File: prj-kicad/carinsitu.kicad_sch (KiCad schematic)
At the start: 65 parts, among them P1 BAT, P2 MOT, P3 CONN_3, P4 CONN_4, SW1 SWITCH_SLIDE, SW2 SW_Push, U1 LoLin_D1_mini_pro, U2 MIC2860, U3 MAX17205, U4 SN74LVC1T45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

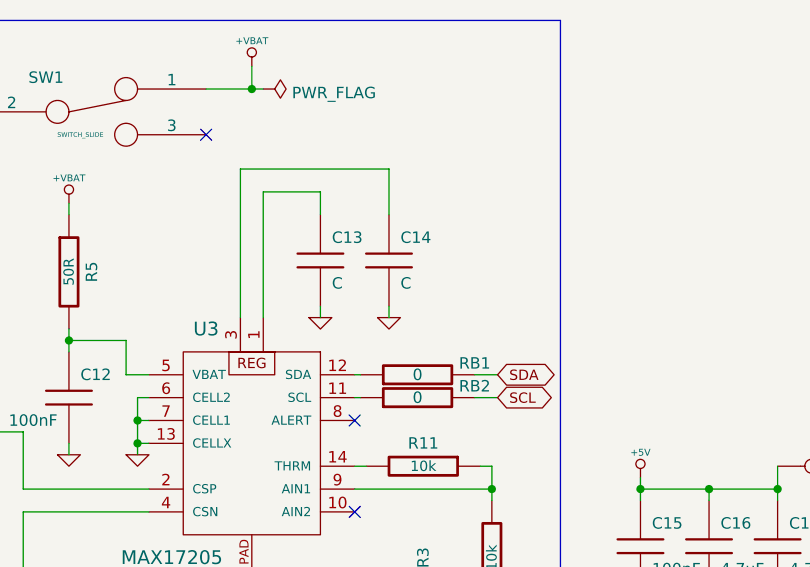
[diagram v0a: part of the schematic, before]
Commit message: review MAX17205 Fuel Gauge Add missing cap values
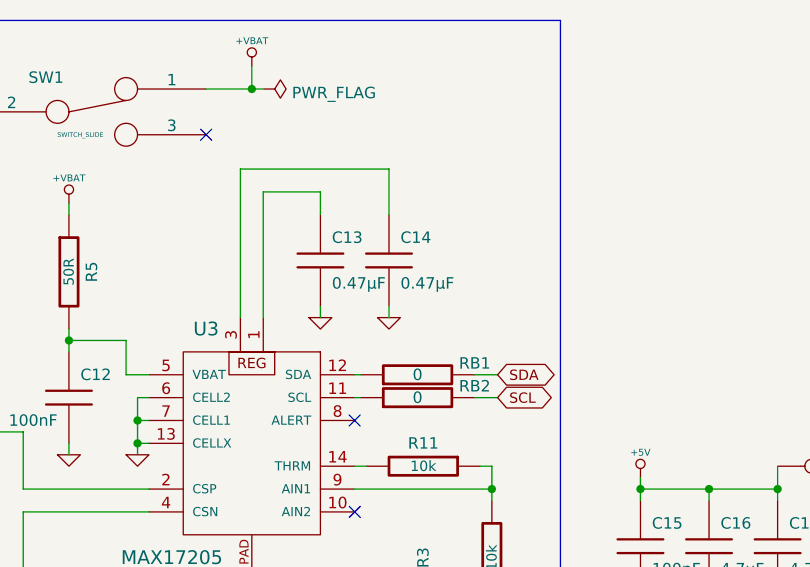
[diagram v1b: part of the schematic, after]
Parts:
- C13, C14: value C -> 0.47µF
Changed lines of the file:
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@@
       (effects (font (size 1.27 1.27)) (justify left))
     )
-    (property "Value" "C" (id 1) (at 74.93 149.86 0)
+    (property "Value" "0.47µF" (id 1) (at 74.93 149.86 0)
       (effects (font (size 1.27 1.27)) (justify left))
     )
@@
       (effects (font (size 1.27 1.27)) (justify left))
     )
-    (property "Value" "C" (id 1) (at 82.55 149.86 0)
+    (property "Value" "0.47µF" (id 1) (at 82.55 149.86 0)
       (effects (font (size 1.27 1.27)) (justify left))
     )
@@
     )
     (path "/00000000-0000-0000-0000-00005d26d447"
-      (reference "C13") (unit 1) (value "C") (footprint "carinsitu:SMD0603")
+      (reference "C13") (unit 1) (value "0.47µF") (footprint "carinsitu:SMD0603")
     )
     (path "/00000000-0000-0000-0000-00005d26d4c0"
-      (reference "C14") (unit 1) (value "C") (footprint "carinsitu:SMD0603")
+      (reference "C14") (unit 1) (value "0.47µF") (footprint "carinsitu:SMD0603")
     )
     (path "/00000000-0000-0000-0000-00005d2c6e10"

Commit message: Update PCB + schematic adjustments
Notable schematic changes:
- change level shifters for SN74LV1T34DBV (simplify routing)
- add fuse inversion protection
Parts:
- removed U4, U8: SN74LVC1T45, carinsitu:SOT23-6, symbol carinsitu:SN74LVC1T45
- added D3: D, Diode_THT:D_A-405_P2.54mm_Vertical_KathodeUp, symbol Device:D
- added F1: Polyfuse, Fuse:Fuse_Bourns_MF-RG500, symbol Device:Polyfuse
- added R14: 10k, carinsitu:SMD0805, symbol carinsitu:R
- added U4, U5: SN74LV1T34DBV, Package_TO_SOT_SMD:SOT-23-5, symbol Logic_LevelTranslator:SN74LV1T34DBV
- C4: value 100nF -> 4.7uF
- R11: footprint carinsitu:SMD0603 -> carinsitu:SMD0805
- RB1, RB2, RB3, RB4, RB5, RB6, RB7, RB8, RB9: footprint (none) -> carinsitu:SMD0603
- SW2: value SW_Push -> Reset
- TP12: value CONN_1 -> INT2
- TP13: value CONN_1 -> INT1
- TP7: value CONN_1 -> PPM_ESC
- TP8: value CONN_1 -> HL_PWM
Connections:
- net +5V: now also U4.5 (VCC), U5.5 (VCC)
- net +VBAT: now also SW1.3; no longer SW1.1
- net GND: now also R14.1, U4.3 (GND), U5.3 (GND)
- net PPM_SERVO: now also U4.2 (A); no longer TP6.1
- net RL_DAT: now also R14.2, U5.2 (A); no longer TP9.1
- net at P1.1 (P1): now also R4.1, U3.2 (CSP), D3.2 (A); no longer SW1.2
- net at P3.1 (P1): now also TP6.1, U4.4 (Y)
- net at D4.4 (DIN): now also TP9.1, U5.4 (Y)
- new net: F1.2, P1.2 (PM)
- new net: D3.1 (K), F1.1, SW1.2
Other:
- note added: "Note: MCU has pullup"
- moved on the sheet: C3, C4, D4, D5, P1, P3, RB8, RB9, SW1, TP12, TP13, TP6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

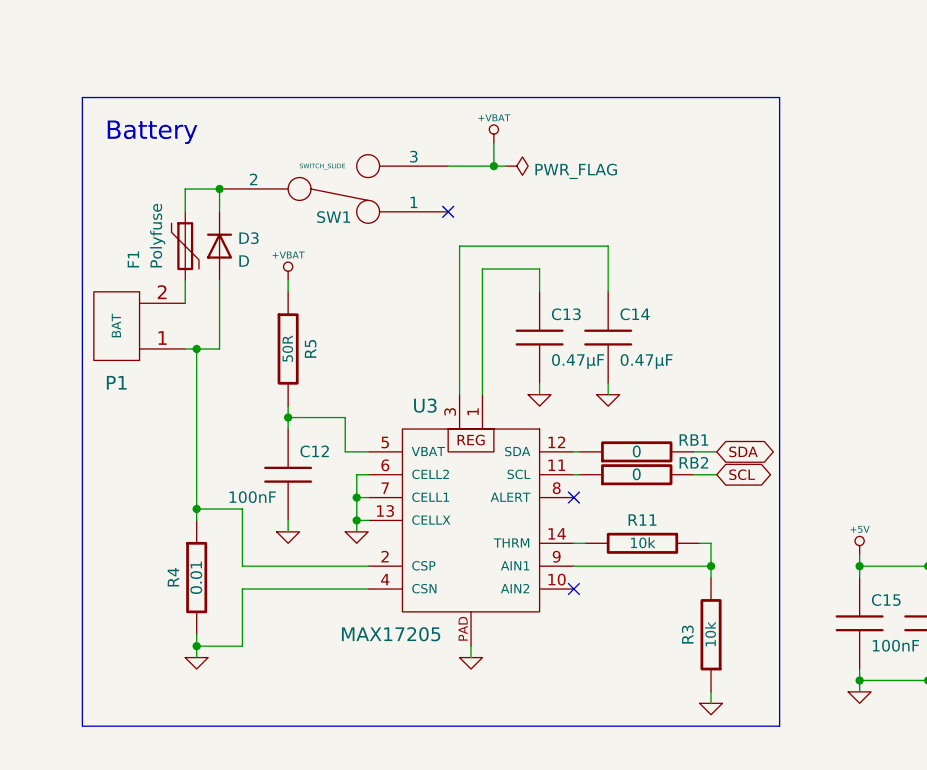
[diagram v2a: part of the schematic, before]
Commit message: Change battery monitor MAX17044G in schematic
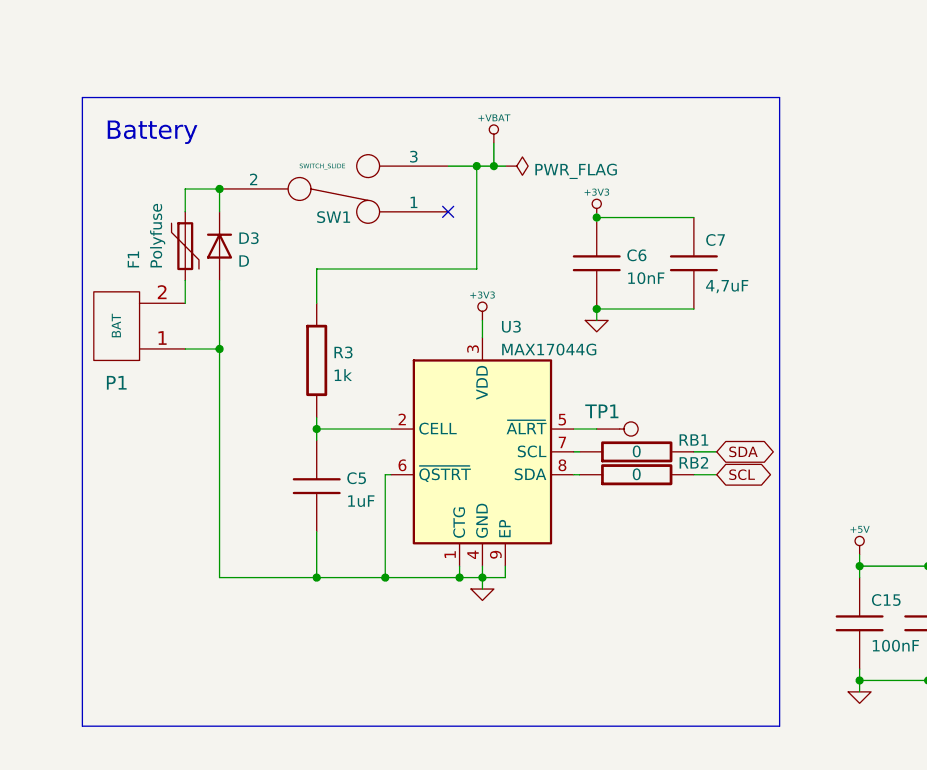
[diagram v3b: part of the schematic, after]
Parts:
- removed C12: 100nF, carinsitu:SMD0603, symbol carinsitu:C
- removed C13, C14: 0.47µF, carinsitu:SMD0603, symbol carinsitu:C
- removed R11: 10k, carinsitu:SMD0805, symbol carinsitu:R
- removed R4: 0.01, carinsitu:SMD0805, symbol carinsitu:R
- removed R5: 50R, carinsitu:SMD0603, symbol carinsitu:R
- removed U3: MAX17205, carinsitu:TDFN14, symbol carinsitu:MAX17205
- added C5: 1uF, carinsitu:SMD0805, symbol carinsitu:C
- added C6: 10nF, carinsitu:SMD0603, symbol carinsitu:C
- added C7: 4,7uF, carinsitu:SMD0805, symbol carinsitu:C
- added TP1: CONN_1, carinsitu:TP, symbol carinsitu:CONN_1
- added U3: MAX17044G, Package_DFN_QFN:TDFN-8-1EP_3x2mm_P0.5mm_EP1.80x1.65mm, symbol carinsitu:MAX17044G
- R3: value 10k -> 1k
- TP12: value INT2 -> CONN_1; RefBis (none) -> INT2
- TP13: value INT1 -> CONN_1; RefBis (none) -> INT1
- TP7: value PPM_ESC -> CONN_1; RefBis (none) -> PPM_ESC
- TP8: value HL_PWM -> CONN_1; RefBis (none) -> HL_PWM
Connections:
- net +3V3: now also C6.1, C7.1, U3.3 (VDD)
- net +VBAT: now also R3.1
- net GND: now also D3.2 (A), P1.1 (P1), C5.2, C6.2, C7.2, U3.1 (CTG), U3.4 (GND), U3.6 (~{QSTRT}), U3.9 (EP); no longer R3.1
- net at R3.2: now also C5.1, U3.2 (CELL)
- net at RB2.1: now also U3.8 (SDA)
- net at RB1.1: now also U3.7 (SCL)
- new net: TP1.1, U3.5 (~{ALRT})
- no-connect marks 6 -> 4

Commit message: Change some footprints for kicad lib ones + silkscreen + route adjustments
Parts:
- C1, C16, C17, C5, C7: footprint carinsitu:SMD0805 -> Capacitor_SMD:C_0805_2012Metric
- C15, C2, C3, C6: footprint carinsitu:SMD0603 -> Capacitor_SMD:C_0603_1608Metric
- C4: footprint carinsitu:SMD0603 -> Capacitor_SMD:C_0805_2012Metric
- D1, D2: footprint carinsitu:LED -> LED_THT:LED_D5.0mm_Horizontal_O3.81mm_Z3.0mm
- R1, R10, R12, R14, R2, R3, R6, R7, R8, R9: footprint carinsitu:SMD0805 -> Resistor_SMD:R_0805_2012Metric
- RB1, RB2, RB3, RB4, RB5, RB6, RB7, RB8, RB9: footprint carinsitu:SMD0603 -> Resistor_SMD:R_0603_1608Metric
- U2: footprint carinsitu:SOT23-6 -> Package_TO_SOT_SMD:SOT-23-6

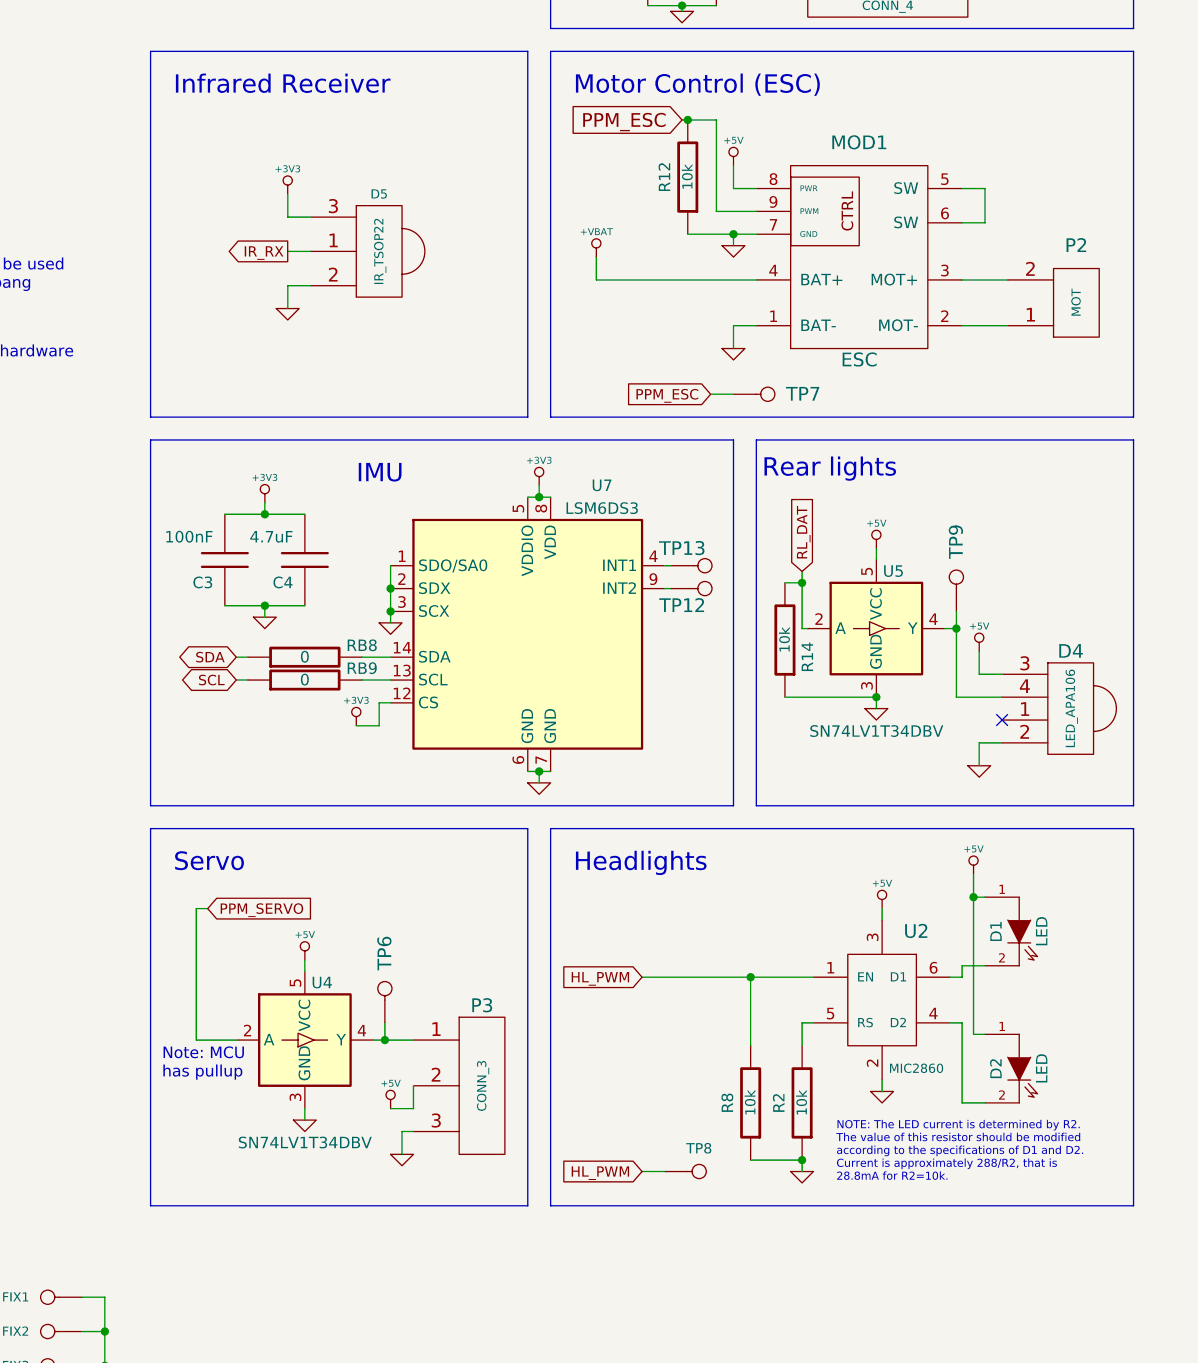
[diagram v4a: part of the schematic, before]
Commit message: Add decoupling capacitors + RB10
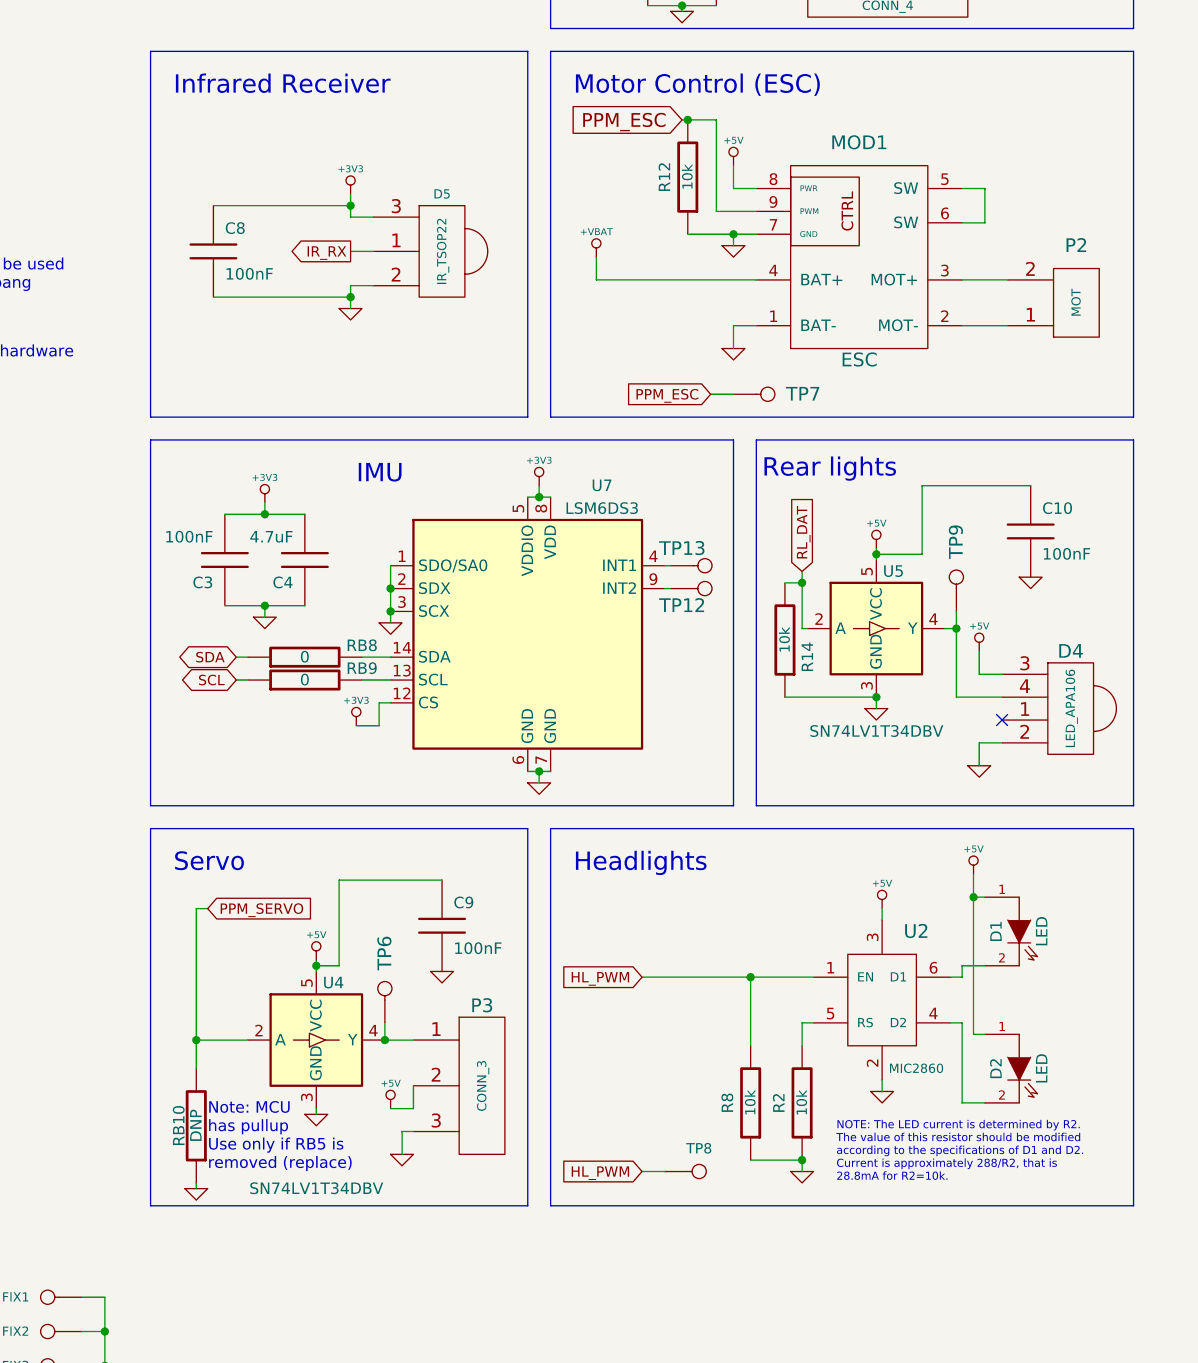
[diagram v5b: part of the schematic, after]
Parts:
- added C10, C8, C9: 100nF, Capacitor_SMD:C_0603_1608Metric, symbol carinsitu:C
- added RB10: DNP, Resistor_SMD:R_0603_1608Metric, symbol carinsitu:R
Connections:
- net +3V3: now also C8.1
- net +5V: now also C10.1, C9.1
- net GND: now also C10.2, C8.2, C9.2, RB10.1
- net PPM_SERVO: now also RB10.2
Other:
- note added: "Note: MCU has pullup Use only if RB5 is removed (replace)"
- note removed: "Note: MCU has pullup"
- moved on the sheet: D5, U4

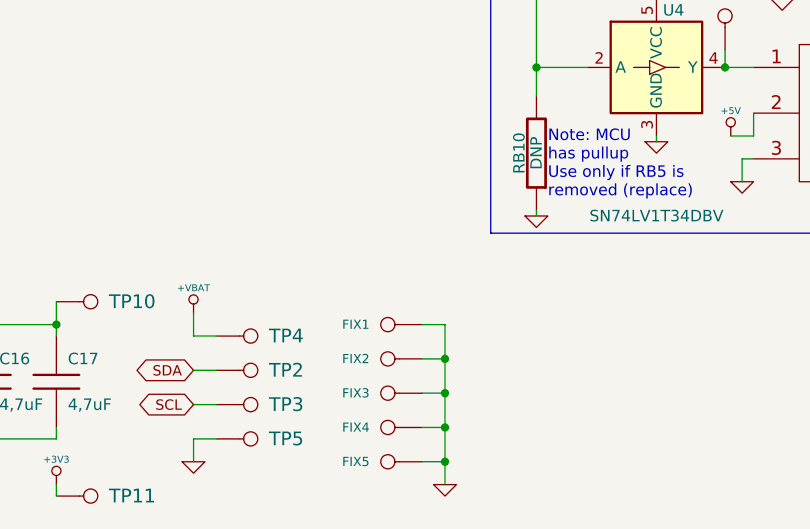
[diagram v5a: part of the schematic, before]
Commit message: Add VTX holes (WIP, bottom right needs rerouting)
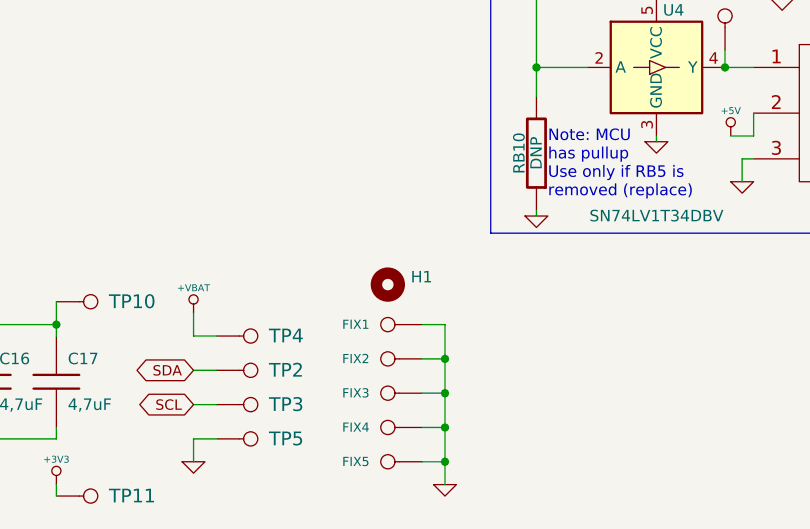
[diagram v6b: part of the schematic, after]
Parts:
- added H1: MountingHole, symbol Mechanical:MountingHole
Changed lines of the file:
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@@
     (pin "1")
+  )
+  (symbol (lib_id "Mechanical:MountingHole") (at 161.29 168.275 0) (unit 1)
+    (in_bom yes) (on_board yes) (fields_autoplaced)
+    (property "Reference" "H1" (id 0) (at 163.83 167.4403 0)
+      (effects (font (size 1.27 1.27)) (justify left))
+    )
+    (property "Value" "MountingHole" (id 1) (at 163.83 169.9772 0)
+      (effects (font (size 1.27 1.27)) (justify left) hide)
+    )
+    (property "Footprint" "" (id 2) (at 161.29 168.275 0)
+      (effects (font (size 1.27 1.27)) hide)
+    )
+    (property "Datasheet" "~" (id 3) (at 161.29 168.275 0)
+      (effects (font (size 1.27 1.27)) hide)
+    )
   )
   (symbol (lib_id "carinsitu:C") (at 235.585 24.13 0) (unit 1)
@@
       (reference "FIX5") (unit 1) (value "CONN_1") (footprint "carinsitu:FIX")
     )
+    (path "/35e83979-c09f-4e93-8e3e-50ecb5934fd1"
+      (reference "H1") (unit 1) (value "MountingHole") (footprint "")
+    )
     (path "/00000000-0000-0000-0000-00005d08f04c"
